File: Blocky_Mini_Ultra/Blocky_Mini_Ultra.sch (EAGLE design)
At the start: 41 parts, among them IC3 MCP1703CB, J1 2P-2.0-90D-SMD, J2 10118193-0001LF, U1 MCP73831, X1 16 MHz, X4 12MHz

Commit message: Update schematic
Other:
- note added: "Mini ULTRA"
- note added: "author: Minh Ha"
- note added: "http://www.getblocky.com"
- note removed: "Moteino MEGA"
- note removed: "author: Felix Rusu"
- note removed: "http://lowpowerlab.com"
- moved on the sheet: C1, C12, C2, C3, C4, C5, C8, C9, D1, IC3, J1, J2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

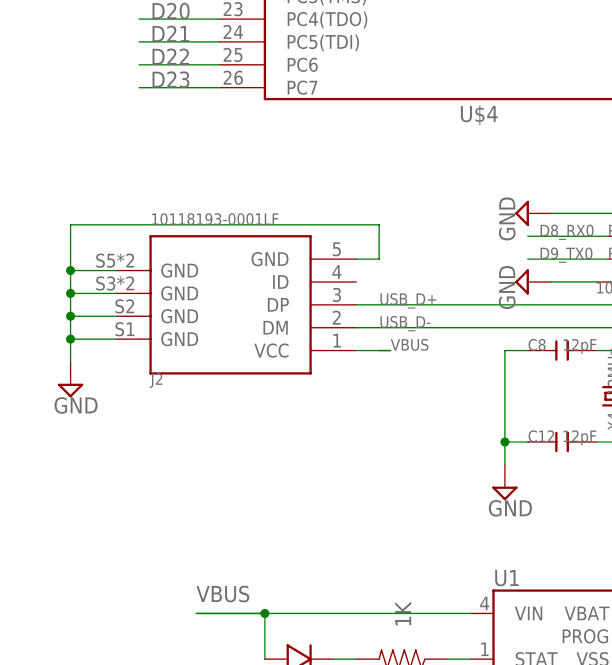
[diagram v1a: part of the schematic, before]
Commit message: Replace usb for mini ultra
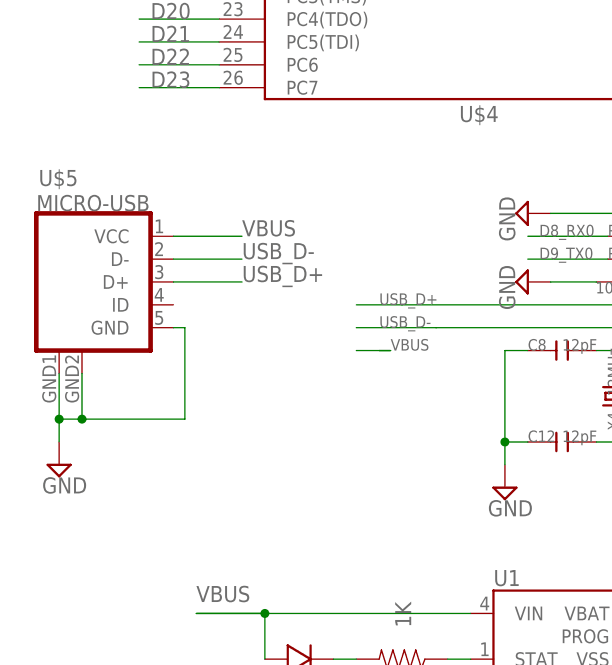
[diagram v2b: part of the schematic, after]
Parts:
- removed J2: 10118193-0001LF, Seeed-Connector -2016:MICRO-USB-SMD-B-(10118193-0001LF)
- added U$5: MICRO-USB, My-Eagle-Lib:MICRO-USB
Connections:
- net GND: now also U$5.GND, U$5.GND@1, U$5.GND@2; no longer J2.GND@1, J2.GND@2, J2.GND@3, J2.GND@4, J2.GND@5
- net USB_D+: now also U$5.D+; no longer J2.DP
- net USB_D-: now also U$5.D-; no longer J2.DM
- net VBUS: now also U$5.VCC; no longer J2.VCC
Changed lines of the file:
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@@
 <part name="U$7" library="adafruit" deviceset="FIDUCIAL" device=""/>
 <part name="J1" library="Seeed-Connector" library_urn="urn:adsk.eagle:library:478" deviceset="CONN-HEADER-SMD-PH-SIDE-(2P-2.0MM)" device="" package3d_urn="urn:adsk.eagle:package:33120/1" value="2P-2.0-90D-SMD"/>
-<part name="J2" library="Seeed-Connector -2016" deviceset="MICRO-USB-SMD-B-(10118193-0001LF)" device="" value="10118193-0001LF"/>
 <part name="U1" library="SparkFun-PowerIC" deviceset="MCP73831" device=""/>
 <part name="R5" library="LowPowerLab" deviceset="RESISTOR" device="0603-RES" value="1K"/>
 <part name="CHG" library="LowPowerLab" deviceset="LED" device="0603" value="RED"/>
 <part name="SUPPLY15" library="supply2" deviceset="GND" device=""/>
-<part name="SUPPLY17" library="supply2" deviceset="GND" device=""/>
 <part name="SUPPLY18" library="supply2" deviceset="GND" device=""/>
 <part name="R6" library="LowPowerLab" deviceset="RESISTOR" device="0603-RES" value="10K"/>
@@
 <part name="C9" library="LowPowerLab" deviceset="CAP" device="0603-CAP" value="0.1u"/>
 <part name="MBR0001" library="adafruit" library_urn="urn:adsk.eagle:library:420" deviceset="DIODE" device="SOD-123" value="MBR120"/>
+<part name="U$5" library="My-Eagle-Lib" deviceset="MICRO-USB" device=""/>
+<part name="SUPPLY21" library="supply2" deviceset="GND" device=""/>
 </parts>
 <sheets>
@@
 <instance part="U$7" gate="G$1" x="25.4" y="10.16"/>
 <instance part="J1" gate="G$1" x="110.49" y="35.56"/>
-<instance part="J2" gate="G$1" x="34.29" y="71.12" smashed="yes" rot="MR180">
-<attribute name="NAME" x="25.4" y="63.5" size="1.27" layer="95" rot="MR180"/>
-<attribute name="VALUE" x="25.4" y="81.28" size="1.27" layer="96" rot="MR180"/>
-</instance>
 <instance part="U1" gate="G$1" x="71.12" y="34.29"/>
 <instance part="R5" gate="G$1" x="53.34" y="31.75" smashed="yes" rot="R180">
@@
 <instance part="CHG" gate="G$1" x="43.18" y="31.75" smashed="yes" rot="R180"/>
 <instance part="SUPPLY15" gate="GND" x="121.92" y="25.4"/>
-<instance part="SUPPLY17" gate="GND" x="16.51" y="62.23"/>
 <instance part="SUPPLY18" gate="GND" x="90.17" y="17.78"/>
 <instance part="R6" gate="G$1" x="90.17" y="27.94" smashed="yes" rot="R270">
@@
 <attribute name="VALUE" x="190.5" y="107.95" size="1.27" layer="96" rot="R270"/>
 </instance>
+<instance part="U$5" gate="G$1" x="12.7" y="81.28"/>
+<instance part="SUPPLY21" gate="GND" x="15.24" y="53.34"/>
 </instances>
 <busses>
@@
 </segment>
 <segment>
-<pinref part="J2" gate="G$1" pin="GND@1"/>
-<wire x1="21.59" y1="67.31" x2="16.51" y2="67.31" width="0.1524" layer="91"/>
-<wire x1="16.51" y1="64.77" x2="16.51" y2="67.31" width="0.1524" layer="91"/>
-<wire x1="16.51" y1="72.39" x2="21.59" y2="72.39" width="0.1524" layer="91"/>
-<pinref part="J2" gate="G$1" pin="GND@3"/>
-<pinref part="J2" gate="G$1" pin="GND@4"/>
-<wire x1="21.59" y1="74.93" x2="16.51" y2="74.93" width="0.1524" layer="91"/>
-<wire x1="16.51" y1="74.93" x2="16.51" y2="72.39" width="0.1524" layer="91"/>
-<pinref part="J2" gate="G$1" pin="GND@2"/>
-<wire x1="21.59" y1="69.85" x2="16.51" y2="69.85" width="0.1524" layer="91"/>
-<wire x1="16.51" y1="69.85" x2="16.51" y2="72.39" width="0.1524" layer="91"/>
-<junction x="16.51" y="72.39"/>
-<wire x1="16.51" y1="67.31" x2="16.51" y2="69.85" width="0.1524" layer="91"/>
-<junction x="16.51" y="67.31"/>
-<junction x="16.51" y="69.85"/>
-<wire x1="16.51" y1="74.93" x2="16.51" y2="80.01" width="0.1524" layer="91"/>
-<junction x="16.51" y="74.93"/>
-<wire x1="16.51" y1="80.01" x2="50.8" y2="80.01" width="0.1524" layer="91"/>
-<wire x1="50.8" y1="80.01" x2="50.8" y2="76.2" width="0.1524" layer="91"/>
-<pinref part="J2" gate="G$1" pin="GND@5"/>
-<wire x1="50.8" y1="76.2" x2="48.26" y2="76.2" width="0.1524" layer="91"/>
-<pinref part="SUPPLY17" gate="GND" pin="GND"/>
-</segment>
-<segment>
 <pinref part="U1" gate="G$1" pin="VSS"/>
 <wire x1="81.28" y1="31.75" x2="85.09" y2="31.75" width="0.1524" layer="91"/>
@@
 <pinref part="GND15" gate="1" pin="GND"/>
 <pinref part="C9" gate="G$1" pin="2"/>
+</segment>
+<segment>
+<pinref part="U$5" gate="G$1" pin="GND"/>
+<wire x1="27.94" y1="68.58" x2="29.21" y2="68.58" width="0.1524" layer="91"/>
+<wire x1="29.21" y1="68.58" x2="29.21" y2="58.42" width="0.1524" layer="91"/>
+<wire x1="29.21" y1="58.42" x2="17.78" y2="58.42" width="0.1524" layer="91"/>
+<pinref part="U$5" gate="G$1" pin="GND@1"/>
+<wire x1="17.78" y1="58.42" x2="15.24" y2="58.42" width="0.1524" layer="91"/>
+<wire x1="15.24" y1="58.42" x2="15.24" y2="63.5" width="0.1524" layer="91"/>
+<pinref part="U$5" gate="G$1" pin="GND@2"/>
+<wire x1="17.78" y1="63.5" x2="17.78" y2="58.42" width="0.1524" layer="91"/>
+<junction x="17.78" y="58.42"/>
+<wire x1="15.24" y1="58.42" x2="15.24" y2="55.88" width="0.1524" layer="91"/>
+<junction x="15.24" y="58.42"/>
+<pinref part="SUPPLY21" gate="GND" pin="GND"/>
 </segment>
 </net>
@@
 <segment>
 <label x="50.8" y="68.58" size="1.27" layer="95"/>
-<pinref part="J2" gate="G$1" pin="DM"/>
 <wire x1="48.26" y1="68.58" x2="57.15" y2="68.58" width="0.1524" layer="91"/>
 <pinref part="U$9" gate="G$1" pin="D-"/>
 <wire x1="87.63" y1="68.58" x2="57.15" y2="68.58" width="0.1524" layer="91"/>
 </segment>
+<segment>
+<pinref part="U$5" gate="G$1" pin="D-"/>
+<wire x1="27.94" y1="76.2" x2="35.56" y2="76.2" width="0.1524" layer="91"/>
+<label x="35.56" y="76.2" size="1.778" layer="95"/>
+</segment>
 </net>
 <net name="USB_D+" class="0">
 <segment>
 <label x="50.8" y="71.12" size="1.27" layer="95"/>
-<pinref part="J2" gate="G$1" pin="DP"/>
 <wire x1="48.26" y1="71.12" x2="53.34" y2="71.12" width="0.1524" layer="91"/>
 <pinref part="U$9" gate="G$1" pin="D+"/>
 <wire x1="53.34" y1="71.12" x2="87.63" y2="71.12" width="0.1524" layer="91"/>
+</segment>
+<segment>
+<pinref part="U$5" gate="G$1" pin="D+"/>
+<wire x1="27.94" y1="73.66" x2="35.56" y2="73.66" width="0.1524" layer="91"/>
+<label x="35.56" y="73.66" size="1.778" layer="95"/>
 </segment>
 </net>
@@
 <segment>
 <label x="52.07" y="66.04" size="1.27" layer="95" ratio="10"/>
-<pinref part="J2" gate="G$1" pin="VCC"/>
 <wire x1="48.26" y1="66.04" x2="52.07" y2="66.04" width="0.1524" layer="91"/>
 <wire x1="52.07" y1="66.04" x2="50.8" y2="66.04" width="0.1524" layer="91"/>
@@
 <label x="30.48" y="38.1" size="1.778" layer="95"/>
 </segment>
-</net>
+<segment>
+<pinref part="U$5" gate="G$1" pin="VCC"/>
+<wire x1="27.94" y1="78.74" x2="35.56" y2="78.74" width="0.1524" layer="91"/>
+<label x="35.56" y="78.74" size="1.778" layer="95"/>
+</segment>
+</net>
